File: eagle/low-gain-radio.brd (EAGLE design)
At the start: 99 x 100 mm, 128 parts, among them U1 MKW01Z128, U2 SKY65116, U3 W25Q80DV, U4 LP5907MFX-3.3, U6 LP5907MFX-3.3, U7 LD39200, U8 MAAL-010704, Y1 32MHz

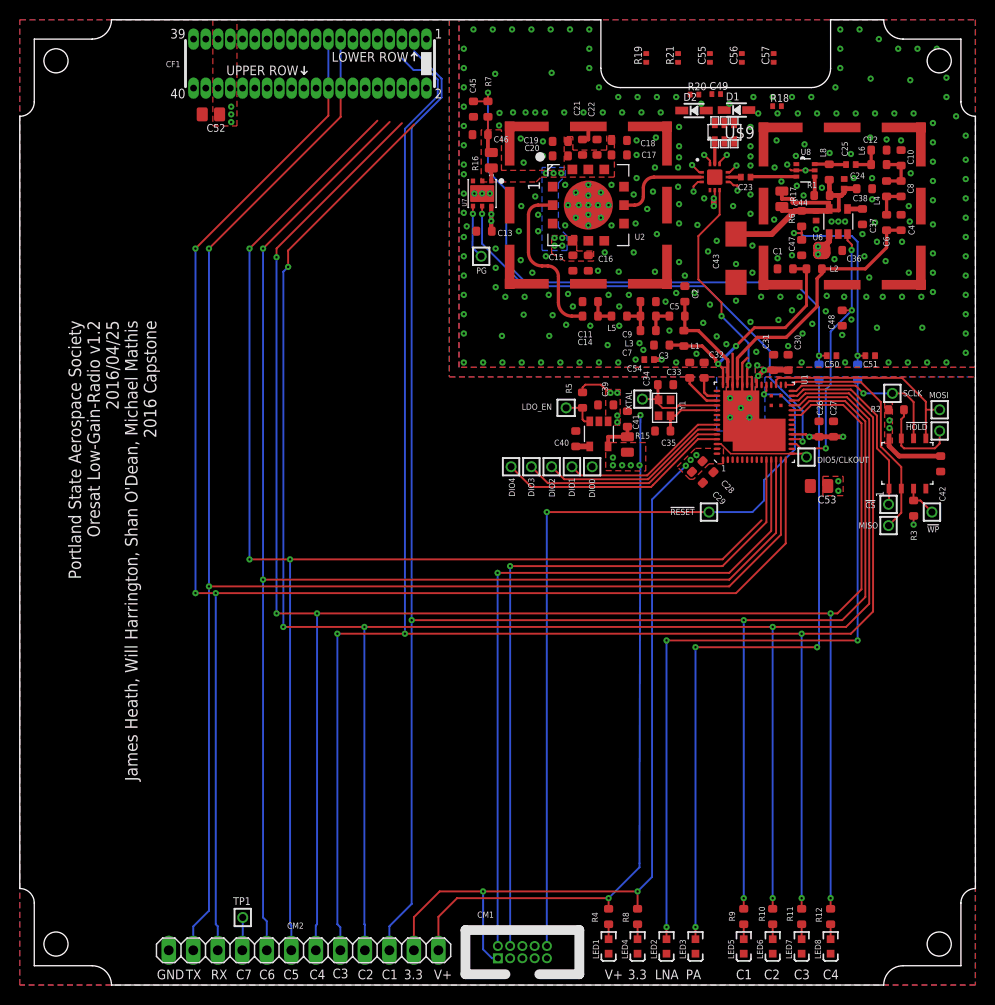
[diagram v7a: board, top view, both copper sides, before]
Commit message: New OreSat card v0.4 layout, meant for internal backplane positioning. Moved to MMCX conncectors. Routed RF reflectometer lines, moved stuff around to get better access to the RF-RESET, and touched up the new zero ohm resistors in all of the power lines.
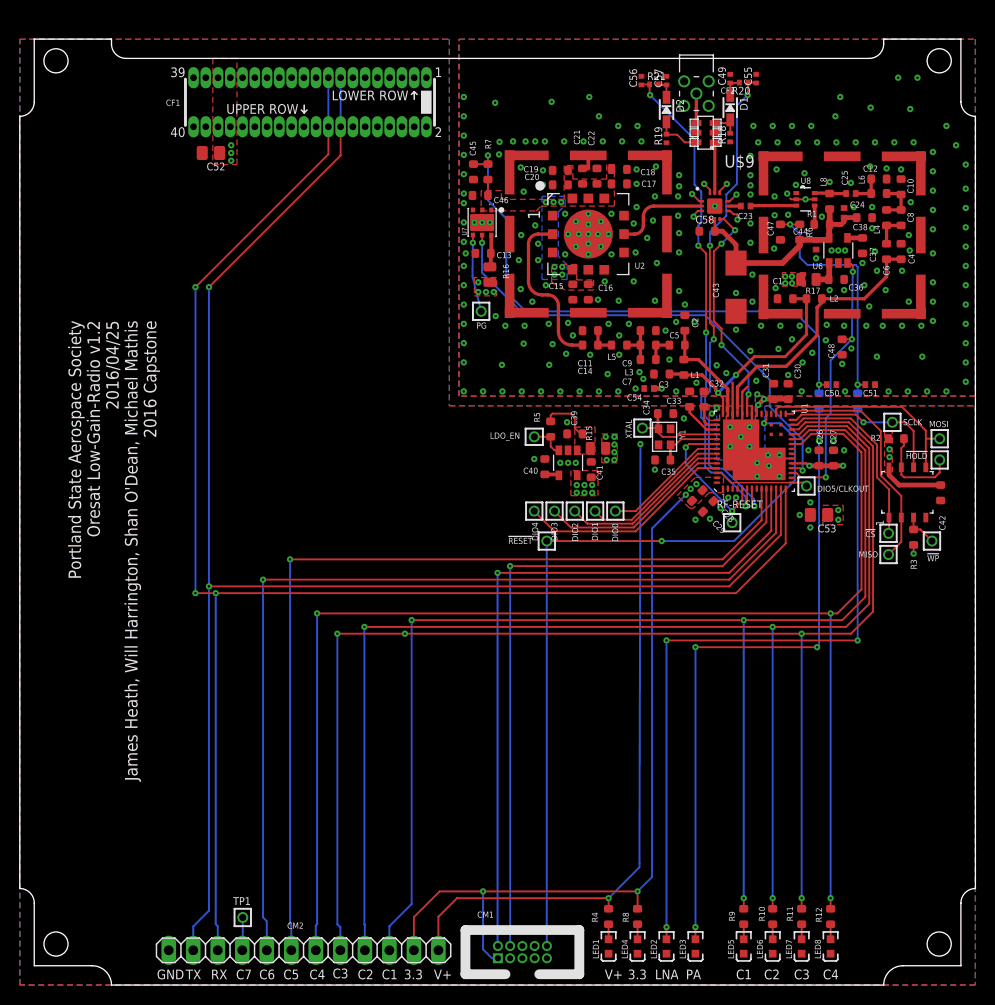
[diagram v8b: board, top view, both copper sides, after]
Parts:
- added C58: 10nF, rcl_custom:.0603-B-NOSILK
- added CF2: CON-MMCX-F-MOLEX-0734151001, oresat-eagle:CON-MMCX-F-MOLEX-0734151001
- added RF-RESET: TEST-POINT, Tova:2MM-TEST-POINT
- U$35: device oresat-eagle:ORESAT-CARD-RF-V0.3 -> oresat-eagle:ORESAT-CARD-RF-V0.4
- moved !RESET 17.1 mm to (54.6, 46.0)
- moved R16 11.9 mm to (48.7, 73.6), turned to 270 degrees
- moved C57 11.3 mm to (67.0, 93.7)
- moved C56 10.7 mm to (64.4, 93.7)
- moved R17 8.79 mm to (81.7, 73.1), turned to 180 degrees
- moved R19 8.61 mm to (67.0, 87.7)
- moved C45 6.50 mm to (47.0, 84.2)
- moved R7 6.50 mm to (48.5, 84.2)
- moved C41 6.45 mm to (59.2, 53.4)
- moved C46 6.30 mm to (47.7, 81.8)
- moved R18 5.84 mm to (73.6, 87.8), turned to 90 degrees
- moved PG 5.70 mm to (47.8, 69.8)
- moved C55 5.26 mm to (76.3, 93.9)
- moved R20 5.25 mm to (75.0, 93.5), turned to 180 degrees
- moved DIO0 5.19 mm to (61.7, 49.1)
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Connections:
- removed net N$11: R17.1, U6.5
- new net N$12: C39.2, R15.1, R5.2, U4.1
- net 3.3V: now also C41.2, C53.1, U4.5; no longer R15.2
- net DC_OUT: now also CF2.CENTER
- net N$6: now also C13.2, R16.1, U7.6; no longer C41.2, C53.1, R15.1, U4.5
- net N$9: now also C36.2, R17.1, U6.1; no longer R16.1, U7.1
- net RF_GND: now also C58.1, CF2.G1, CF2.G2, CF2.G3, CF2.G4
- net RF_RESET: now also RF-RESET.1
- net V+: now also R15.2, R16.2, R17.2; no longer C13.2, C36.2, C39.2, R5.2, U$9.5, U4.1, U6.1, U7.6
- net VBIAS: now also C58.2, U$9.5, U6.5; no longer R17.2
- net VPA: now also U7.1; no longer R16.2
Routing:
- net PTC2: track 210.5 -> 141.4 mm, vias 5 -> 3
- net PTC3: track 211.2 -> 144.8 mm
- net PTC1: track 201.5 -> 137.1 mm
- net PTC4: track 209.0 -> 145.6 mm, vias 5 -> 3
- net PTA4: track 154.1 -> 98.3 mm, vias 2 -> 1
- net VFWD: track 0.00 -> 51.9 mm, vias 0 -> 4
- net PTE30: track 146.2 -> 94.4 mm, vias 3 -> 1
- net VREV: track 0.00 -> 51.6 mm, vias 0 -> 4
- net V+: track 88.4 -> 72.3 mm, vias 16 -> 20
- net RF_RESET: track 0.00 -> 15.9 mm, vias 0 -> 2
- net DIO0: track 0.00 -> 13.2 mm
- net UART0_TX: track 170.0 -> 163.0 mm
- net UART0_RX: track 172.1 -> 165.1 mm
- net N$11: track 6.75 -> 0.00 mm
- net N$12: track 0.00 -> 5.50 mm
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- added copper zone on layer 1, net N$12
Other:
- board size 99 x 100 mm -> 99 x 98 mm
